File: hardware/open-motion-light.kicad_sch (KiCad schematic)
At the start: 95 parts, among them J1 TYPE-C-31-M-12, Q1 2N7002, SW1 SW_Push, SW3 SSSS213800, U1 CN3058E, U2 VCNL4020-GS08, U3 MT9284BS6, U4 PIR223D-S0, U6 CH340X, U7 STM32L051K8Ux

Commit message: Tentative hardware v1.2
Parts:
- removed U4: PIR223D-S0, Homebrew:PIR223D-S0, symbol Homebrew:PIR223D-S0
- added C22: 47uF, Capacitor_SMD:C_1206_3216Metric, symbol Device:C
- added R41: 2M, Resistor_SMD:R_0603_1608Metric, symbol Device:R
- added R42: 330k, Resistor_SMD:R_0603_1608Metric, symbol Device:R
- added U4: XYC-PIR224S-S1, Homebrew:TO-5-4_BD9.2-P2.54_XYC-PIR224D-D0, symbol Homebrew:XYC-PIR224S-S1
- R39: footprint Resistor_SMD:R_0603_1608Metric -> Resistor_SMD:R_0402_1005Metric
- R40: value 1k -> 10k; footprint Resistor_SMD:R_0402_1005Metric -> Resistor_SMD:R_0603_1608Metric_Pad0.98x0.95mm_HandSolder; LCSC C11702 -> C25804
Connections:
- net GND: now also C22.1, R41.2, U4.1 (VSS)
- net PIR: now also R17.1, R26.1; no longer R26.2
- net at C14.1, C21.1, R40.2: now also C22.2, R42.1, U4.3 (VDD)
- new net: R41.1, R42.2, U4.2 (SENS)
- new net: R26.2, U4.4 (REL)
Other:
- note added: "SENS max: 1/4 * Vdd = 0.825V Voltage divider: 0.467V"
- note added: "T=0.57s Power consumption: max 10uA Voltage drop: max 100mV"
- note removed: "T=10ms Power consumption: 10uA Voltage drop: 10mV"
- moved on the sheet: C14, C17, C21, C4, C5, C6, C7, R13, R17, R26, R39, R40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

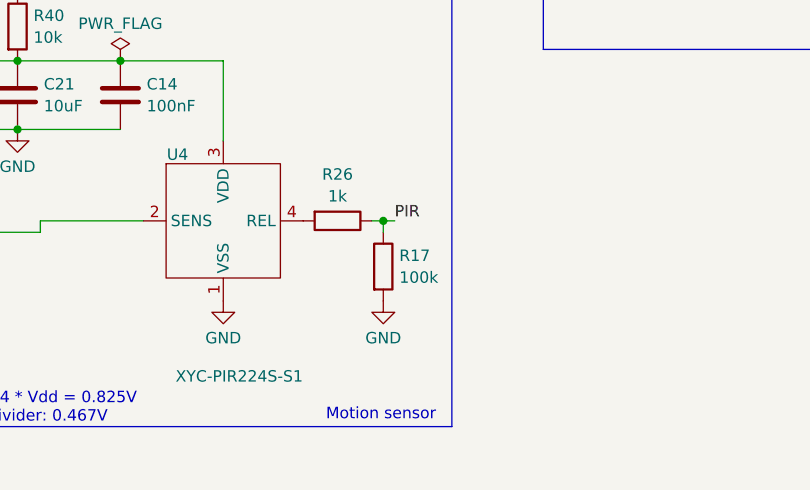
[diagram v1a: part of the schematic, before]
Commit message: v1.2: remove PIR pulldown
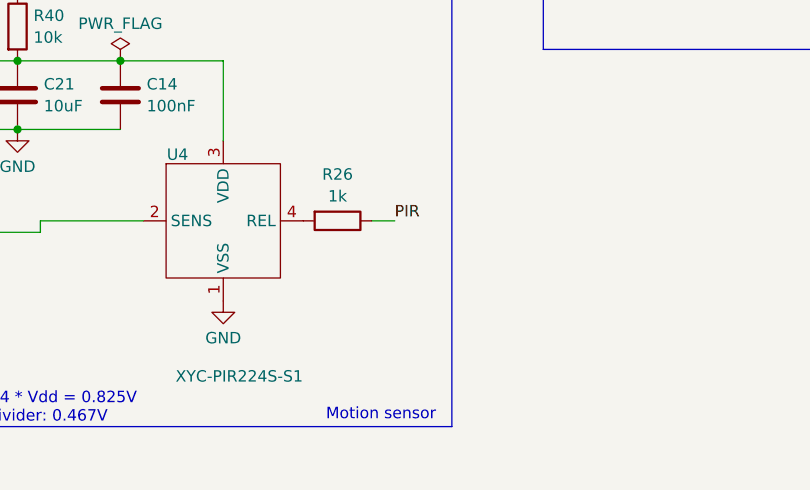
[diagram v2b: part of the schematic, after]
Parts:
- removed R17: 100k, Resistor_SMD:R_0402_1005Metric, symbol Device:R
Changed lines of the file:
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@@
 	)
 	(junction
-		(at 171.45 248.92)
-		(diameter 0)
-		(color 0 0 0 0)
-	)
-	(junction
 		(at 69.85 105.41)
 		(diameter 0)
@@
 	(wire
 		(pts
-			(xy 172.72 248.92) (xy 171.45 248.92)
+			(xy 170.18 248.92) (xy 172.72 248.92)
 		)
 		(stroke
@@
 	(wire
 		(pts
-			(xy 171.45 248.92) (xy 170.18 248.92)
-		)
-		(stroke
-			(width 0)
-			(type default)
-		)
-	)
-	(wire
-		(pts
 			(xy 38.1 218.44) (xy 45.72 218.44)
 		)
@@
 	(wire
 		(pts
-			(xy 171.45 250.19) (xy 171.45 248.92)
-		)
-		(stroke
-			(width 0)
-			(type default)
-		)
-	)
-	(wire
-		(pts
 			(xy 39.37 180.34) (xy 49.53 180.34)
 		)
@@
 	)
 	(symbol
-		(lib_id "Device:R")
-		(at 171.45 254 0)
-		(unit 1)
-		(exclude_from_sim no)
-		(in_bom yes)
-		(on_board yes)
-		(dnp no)
-		(fields_autoplaced yes)
-		(property "Reference" "R17"
-			(at 173.228 252.7878 0)
-			(effects
-				(font
-					(size 1.27 1.27)
-				)
-				(justify left)
-			)
-		)
-		(property "Value" "100k"
-			(at 173.228 255.2121 0)
-			(effects
-				(font
-					(size 1.27 1.27)
-				)
-				(justify left)
-			)
-		)
-		(property "Footprint" "Resistor_SMD:R_0402_1005Metric"
-			(at 169.672 254 90)
-			(effects
-				(font
-					(size 1.27 1.27)
-				)
-				(hide yes)
-			)
-		)
-		(property "Datasheet" "~"
-			(at 171.45 254 0)
-			(effects
-				(font
-					(size 1.27 1.27)
-				)
-				(hide yes)
-			)
-		)
-		(property "Description" "Resistor"
-			(at 171.45 254 0)
-			(effects
-				(font
-					(size 1.27 1.27)
-				)
-				(hide yes)
-			)
-		)
-		(property "LCSC" "C25741"
-			(at 171.45 254 0)
-			(effects
-				(font
-					(size 1.27 1.27)
-				)
-				(hide yes)
-			)
-		)
-		(pin "2"
-		)
-		(pin "1"
-		)
-		(instances
-			(project "open-motion-light"
-				(path "/f39d6745-1b59-458d-9712-dda63c04ccc8"
-					(reference "R17")
-					(unit 1)
-				)
-			)
-		)
-	)
-	(symbol
 		(lib_id "power:GND")
 		(at 36.83 187.96 0)
@@
 					(unit 1)
 				)
-			)
-		)
-	)
-	(symbol
-		(lib_id "power:GND")
-		(at 171.45 257.81 0)
-		(unit 1)
-		(exclude_from_sim no)
-		(in_bom yes)
-		(on_board yes)
-		(dnp no)
-		(fields_autoplaced yes)
-		(property "Reference" "#PWR038"
-			(at 171.45 264.16 0)
-			(effects
-				(font
-					(size 1.27 1.27)
-				)
-				(hide yes)
-			)
-		)
-		(property "Value" "GND"
-			(at 171.45 261.9431 0)
-			(effects
-				(font
-					(size 1.27 1.27)
-				)
-			)
-		)
-		(property "Footprint" ""
-			(at 171.45 257.81 0)
-			(effects
-				(font
-					(size 1.27 1.27)
-				)
-				(hide yes)
-			)
-		)
-		(property "Datasheet" ""
-			(at 171.45 257.81 0)
-			(effects
-				(font
-					(size 1.27 1.27)
-				)
-				(hide yes)
-			)
-		)
-		(property "Description" "Power symbol creates a global label with name \"GND\" , ground"
-			(at 171.45 257.81 0)
-			(effects
-				(font
-					(size 1.27 1.27)
-				)
-				(hide yes)
-			)
-		)
-		(pin "1"
-		)
-		(instances
-			(project "open-motion-light"
-				(path "/f39d6745-1b59-458d-9712-dda63c04ccc8"
-					(reference "#PWR038")
-					(unit 1)
-				)

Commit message: Hardware v1.2
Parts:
- added C23: 100nF, Capacitor_SMD:C_0402_1005Metric, symbol Device:C
- added C24: 10uF, Capacitor_SMD:C_0603_1608Metric, symbol Device:C
- C1: value 4.7uF -> 47uF; footprint Capacitor_SMD:C_0603_1608Metric -> Capacitor_SMD:C_1206_3216Metric; LCSC C19666 -> C96123
- R42: now not fitted
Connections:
- net +5V: now also C1.2, C23.2, C24.1; no longer C1.1
- net GND: now also C1.1, C23.1, C24.2; no longer C1.2
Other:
- moved on the sheet: BT1, C3, C8, D13, D6, F1, Q1, R1, R10, R2, R3, R32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

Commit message: Hardware v1.3 first pass
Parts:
- added C25, C26, C28: 100nF, Capacitor_SMD:C_0402_1005Metric, symbol Device:C
- added C27: 10uF, Capacitor_SMD:C_0603_1608Metric, symbol Device:C
- added R17: 4M7, Resistor_SMD:R_0603_1608Metric, symbol Device:R
- added U5: DS8561-30D4, Homebrew:UDFN-4_L1.0-W1.0-P0.65-TL, symbol Homebrew:DS8561-30D4
- C22: value 47uF -> 100nF; footprint Capacitor_SMD:C_1206_3216Metric -> Capacitor_SMD:C_0402_1005Metric; LCSC C96123 -> C307331
- R21: value 220 -> 2M; footprint Resistor_SMD:R_0402_1005Metric -> Resistor_SMD:R_0603_1608Metric; LCSC C25091 -> C422964
- R22: value 220 -> 100k; LCSC C25091 -> C25741
- R40: value 10k -> 1M; footprint Resistor_SMD:R_0603_1608Metric_Pad0.98x0.95mm_HandSolder -> Resistor_SMD:R_0603_1608Metric; LCSC C25804 -> C7250
- R41: value 2M -> 1M; LCSC C22976 -> C7250
- R42: value 330k -> 1M; LCSC C23137 -> C7250; now fitted
- U4: footprint Homebrew:TO-5-4_BD9.2-P2.54_XYC-PIR224D-D0 -> easyeda2kicad:TO-5-4_BD9.2-P2.54_XYC-PIR224D-D0
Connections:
- net GND: now also C22.2, R42.2, C25.2, C26.2, C27.2, C28.2, R17.1, U5.2 (GND), U5.5 (SGND); no longer C22.1, R41.2
- net USART_RX: now also U6.8 (TXD); no longer R21.2
- net USART_TX: now also U6.9 (RXD); no longer R22.2
- net VCC: now also C26.1, C27.1, U5.4 (VIN); no longer R40.1
- net at C14.1, R40.2, R42.1: now also R21.2, R41.2, U4.2 (SENS); no longer C21.1, C22.2, U4.3 (VDD)
- net SENS_ADJUST_LOW: now reaches R21.1
- net SENS_ADJUST_LOW: now also U7.23 (PA13); no longer U6.8 (TXD)
- net PIR_EN: now reaches R22.1
- net PIR_EN: now also U7.22 (PA12); no longer U6.9 (RXD)
- net SENS_ADJUST_HIGH_1: now reaches U7.24 (PA14)
- net SENS_ADJUST_HIGH_1: now also R40.1
- net SENS_ADJUST_HIGH_2: now reaches U7.25 (PA15)
- net SENS_ADJUST_HIGH_2: now also R41.1
- new net PIR_3V: C21.1, C22.1, C25.1, U4.3 (VDD), U5.1 (VOUT)
- new net PIR_EN_RAW: C28.1, R17.2, R22.2, U5.3 (EN)
- no-connect marks 13 -> 9
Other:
- note added: "Note: ADC has equivalent ~120kΩ pulldown. SENS max: 1/4 * 3.0V = 0.75V"
- note removed: "SENS max: 1/4 * Vdd = 0.825V Voltage divider: 0.467V"
- note removed: "T=0.57s Power consumption: max 10uA Voltage drop: max 100mV"
- moved on the sheet: C17, C21, C4, C5, C6, C7, R13, R26, R39, SW1, U4, U7

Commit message: WIP start updating for sourcing
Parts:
- removed C22, C26, C28: 100nF, Capacitor_SMD:C_0402_1005Metric, symbol Device:C
- removed C27: 10uF, Capacitor_SMD:C_0603_1608Metric, symbol Device:C
- removed Q1: 2N7002, Package_TO_SOT_SMD:SOT-23, symbol Transistor_FET:2N7002
- removed R10: 100, Resistor_SMD:R_0402_1005Metric, symbol Device:R
- removed R17: 4M7, Resistor_SMD:R_0603_1608Metric, symbol Device:R
- removed R22: 100k, Resistor_SMD:R_0402_1005Metric, symbol Device:R
- removed R32: 22k, Resistor_SMD:R_0402_1005Metric, symbol Device:R
- removed R33: 330k, Resistor_SMD:R_0603_1608Metric, symbol Device:R
- removed U1: CN3058E, Homebrew:SOP-8_3.9x4.9mm_P1.27mm_Thermal, symbol Homebrew:CN3058E
- removed U5: DS8561-30D4, Homebrew:UDFN-4_L1.0-W1.0-P0.65-TL, symbol Homebrew:DS8561-30D4
- added R43: 82k, Resistor_SMD:R_0402_1005Metric, symbol Device:R
- added U1: BQ25170DSGR, DSG0008A, symbol Homebrew:BQ25170DSGR
- R1: value 24k -> 620; LCSC C23352 -> (none)
- R2: value 1k5 -> 1k; footprint Resistor_SMD:R_0603_1608Metric -> Resistor_SMD:R_0402_1005Metric; LCSC C22843 -> C11702
- TH1: footprint Resistor_SMD:R_0402_1005Metric -> Resistor_SMD:R_0603_1608Metric; LCSC C279702 -> C279936
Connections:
- net +5V: now also U1.1 (IN); no longer C1.2
- net GND: now also R43.2, U1.4 (GND), U1.9 (PAD); no longer R3.2
- net PIR_3V: now also C1.2, R3.2
- net TEMP: now also R2.2, U7.15 (PB1); no longer TH1.1
- net VCC: now also R3.1, U1.8 (OUT)
- net at R1.1: now also U1.2 (ISET); no longer R2.1
- net at R6.2, R9.2: now also U1.6 (PG_N)
- net at R7.2, R8.2: now also U1.5 (STAT)
- net CHARGE_HI_ENABLE: no longer names the net of U7.27 (PB4)
- net ~{CHRG} renamed ~{PG}
- net ~{DONE} renamed STAT
- new net: R2.1, TH1.1, U1.3 (TS)
- new net: R43.1, U1.7 (VSET)
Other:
- note added: "480mA charging current V_{SET} = 3.6V, LiFePO4"
- note added: "Battery charge temp: 0C to 50C R=10k at 25C, B=3950K Programmed range: 4C to 42C"
- note added: "Note: ADC has equivalent ~120kΩ pulldown. SENS max: 1/4 * 3.1V = 0.78V"
- note added: "T=0.57s Power consumption: max 10uA Voltage drop: max 100mV"
- note added: "open-motion-light v1.3"
- note removed: "450mA/900mA charging current"
- note removed: "Battery charge temp: 0C to 50C R=47k at 25C, B=4050K At 5C, R=125kΩ At 45C, R=20kΩ"
- note removed: "Note: ADC has equivalent ~120kΩ pulldown. SENS max: 1/4 * 3.0V = 0.75V"
- note removed: "TODO: connect shield?"
- moved on the sheet: BT1, C10, C11, C13, C14, C21, C23, C24, C25, C3, C8, C9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

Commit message: Schematic updates for v1.3 (again)
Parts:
- removed R38: 100k, Resistor_SMD:R_0402_1005Metric, symbol Device:R
- removed U3: MT9284BS6, Homebrew:SOT-23-6_L2.9-W1.6-P0.95-LS2.8-BR, symbol Homebrew:MT9284BS6
- added C22, C26, C27, C28: 100nF, Capacitor_SMD:C_0402_1005Metric, symbol Device:C
- added U3: TPS61165DRV, Package_SON:WSON-6-1EP_2x2mm_P0.65mm_EP1x1.6mm, symbol Driver_LED:TPS61165DRV
- C11: value 10uF 28V -> 4.7uF 50V; LCSC C13585 -> C51205
- F1: value BSMD1206-100-6V -> BSMD1206-075-6V; LCSC C883129 -> C883127
- R1: LCSC (none) -> C23220
- R21: LCSC C422964 -> C22976
- R25: value 5Ω1 -> 4Ω3; LCSC C25197 -> C2933230
- R43: LCSC (none) -> C2909388
- U1: footprint DSG0008A -> Package_SON:Texas_DSG0008A_WSON-8-1EP_2x2mm_P0.5mm_EP0.9x1.6mm_ThermalVias; LCSC (none) -> C5208201
- U4: LCSC (none) -> C6081347
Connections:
- net GND: now also C22.2, C26.2, C27.2, C28.1, U3.3 (GND), U3.7 (GND)
- net VCC: now also C28.2, U3.6 (VIN)
- net at D8.2 (A), L2.1: now also U3.4 (SW)
- net at R34.1: now also U3.5 (CTRL)
- net at C11.1, D8.1 (K), LED1.2: now also C27.1
- net at LED6.1, R25.1: now also U3.1 (FB)
- net PIR_EN: no longer names the net of U7.22 (PA12)
- new net: C22.1, C26.1, U3.2 (COMP)
- no-connect marks 9 -> 10
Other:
- note added: "750mA Polyfuse"
- note added: "V_{FB}=200mV R_{CS}=.2V / 4.3Ω = 47mA Power: .2V * 47mA = 9mW"
- note removed: "1A Polyfuse"
- note removed: "V_{FB}=250mV R_{CS}=.25V / 5.2Ω = 48mA Power: .25V * 48mA = 12mW"
- moved on the sheet: BT1, C10, C11, C13, C14, C17, C3, C4, C5, C6, C7, C8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

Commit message: Hardware v1.3 final
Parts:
- L2: value MPL2016S4R7MHT -> 22uH; footprint Homebrew:L0806 -> Inductor_SMD:L_Sunlord_SWPA4030S; LCSC Part C98335 -> C83472
- R1: footprint Resistor_SMD:R_0603_1608Metric -> Resistor_SMD:R_0603_1608Metric_Pad0.98x0.95mm_HandSolder
- R40, R41, R42: LCSC C7250 -> C22935
- U1: footprint Package_SON:Texas_DSG0008A_WSON-8-1EP_2x2mm_P0.5mm_EP0.9x1.6mm_ThermalVias -> Homebrew:Texas_DSG0008A_WSON-8-1EP_2x2mm_P0.5mm_EP0.9x1.6mm_ThermalVias
- U3: footprint Package_SON:WSON-6-1EP_2x2mm_P0.65mm_EP1x1.6mm -> Homebrew:WSON-6-1EP_2x2mm_P0.65mm_EP1x1.6mm_ThermalVias
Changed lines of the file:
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@@
 			)
 		)
-		(property "Value" "MPL2016S4R7MHT"
+		(property "Value" "22uH"
 			(at 374.65 60.706 0)
 			(effects
@@
 			)
 		)
-		(property "Footprint" "Homebrew:L0806"
+		(property "Footprint" "Inductor_SMD:L_Sunlord_SWPA4030S"
 			(at 374.65 55.88 0)
 			(effects
@@
 			)
 		)
-		(property "Datasheet" "https://lcsc.com/product-detail/Inductors-SMD_4-7uH-20_C98335.html"
+		(property "Datasheet" "https://jlcpcb.com/partdetail/Sunlord-SWPA4030S220MT/C83472"
 			(at 374.65 53.34 0)
 			(effects
@@
 			)
 		)
-		(property "Description" ""
+		(property "Description" "SWPA4030S220MT"
 			(at 374.65 63.5 0)
 			(effects
@@
 			)
 		)
-		(property "LCSC Part" "C98335"
+		(property "LCSC Part" "C83472"
 			(at 374.65 50.8 0)
 			(effects
@@
 			)
 		)
-		(property "Footprint" "Resistor_SMD:R_0603_1608Metric"
+		(property "Footprint" "Resistor_SMD:R_0603_1608Metric_Pad0.98x0.95mm_HandSolder"
 			(at 52.578 113.03 90)
 			(effects
@@
 			)
 		)
-		(property "LCSC" "C7250"
+		(property "LCSC" "C22935"
 			(at 142.24 247.65 0)
 			(effects
@@
 			)
 		)
-		(property "LCSC" "C7250"
+		(property "LCSC" "C22935"
 			(at 148.59 255.27 0)
 			(effects
@@
 			)
 		)
-		(property "Footprint" "Package_SON:Texas_DSG0008A_WSON-8-1EP_2x2mm_P0.5mm_EP0.9x1.6mm_ThermalVias"
+		(property "Footprint" "Homebrew:Texas_DSG0008A_WSON-8-1EP_2x2mm_P0.5mm_EP0.9x1.6mm_ThermalVias"
 			(at 85.09 102.87 0)
 			(effects
@@
 			)
 		)
-		(property "LCSC" "C7250"
+		(property "LCSC" "C22935"
 			(at 149.86 243.84 0)
 			(effects
@@
 			)
 		)
-		(property "Footprint" "Package_SON:WSON-6-1EP_2x2mm_P0.65mm_EP1x1.6mm"
+		(property "Footprint" "Homebrew:WSON-6-1EP_2x2mm_P0.65mm_EP1x1.6mm_ThermalVias"
 			(at 374.65 103.886 0)
 			(effects
